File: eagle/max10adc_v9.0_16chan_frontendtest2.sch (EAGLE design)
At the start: 189 parts, among them IC1 MAX11115AUT+T, IC2 MAX11115AUT+T, IC3 OPA4322AIPWR, IC4 MAX11115AUT+T, IC5 MAX11115AUT+T, K1 AQY21SOP, K3 AQY21SOP, K5 AQY21SOP, K6 AQY21SOP, U340G CH340G, X1 LTI-SASF54GT, X4 LTI-SASF54GT, X5 LTI-SASF54GT, X6 LTI-SASF54GT, Y1 ABL-12.000MHZ-B2

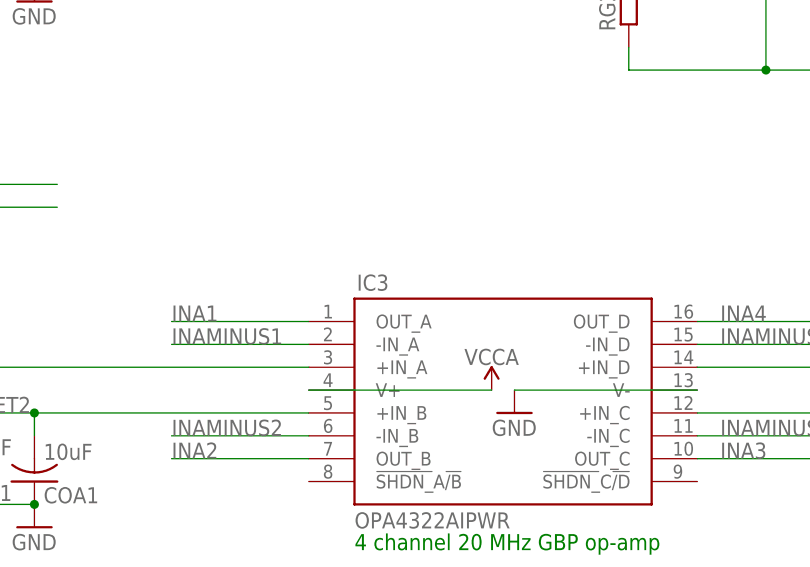
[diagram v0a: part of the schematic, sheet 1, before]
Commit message: 2msps working
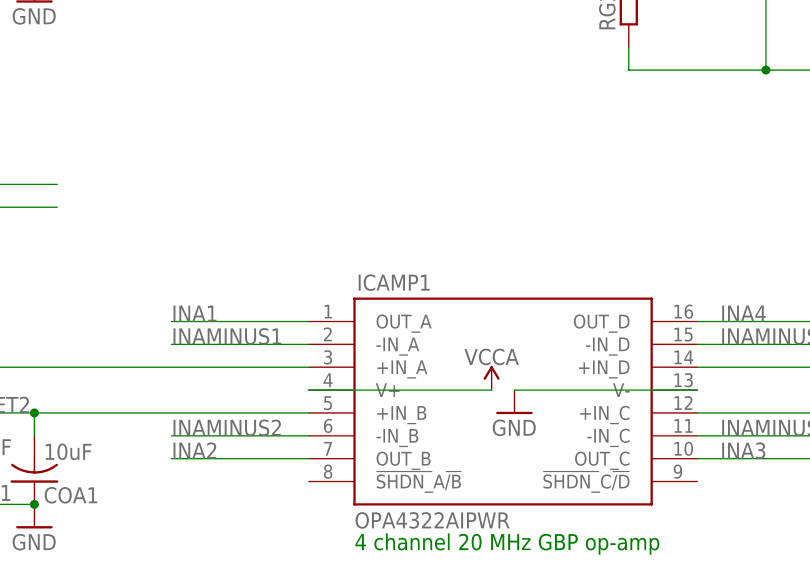
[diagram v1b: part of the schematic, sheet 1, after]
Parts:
- removed IC5: MAX11115AUT+T, SamacSys_Parts:MAX11115AUT+T
- added ICAMP1: OPA4322AIPWR, SamacSys_Parts:OPA4322AIPWR
- IC3: value OPA4322AIPWR -> MAX11115AUT+T; device SamacSys_Parts:OPA4322AIPWR -> SamacSys_Parts:MAX11115AUT+T
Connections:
- net CLKOUT_32: now also IC3.SCLK; no longer IC5.SCLK
- net CLKOUT_33: now also IC3.~CS; no longer IC5.~CS
- net D2A: now also IC3.DOUT; no longer IC5.DOUT
- net GND: now also IC3.GND, ICAMP1.V-; no longer IC3.V-, IC5.GND
- net INA1: now also ICAMP1.OUT_A; no longer IC3.OUT_A
- net INA2: now also ICAMP1.OUT_B; no longer IC3.OUT_B
- net INA3: now also IC3.AIN, ICAMP1.OUT_C; no longer IC3.OUT_C, IC5.AIN
- net INA4: now also ICAMP1.OUT_D; no longer IC3.OUT_D
- net INAMINUS1: now also ICAMP1.-IN_A; no longer IC3.-IN_A
- net INAMINUS2: now also ICAMP1.-IN_B; no longer IC3.-IN_B
- net INAMINUS3: now also ICAMP1.-IN_C; no longer IC3.-IN_C
- net INAMINUS4: now also ICAMP1.-IN_D; no longer IC3.-IN_D
- net OFFSET1: now also ICAMP1.+IN_A; no longer IC3.+IN_A
- net OFFSET2: now also ICAMP1.+IN_B; no longer IC3.+IN_B
- net OFFSET3: now also ICAMP1.+IN_C; no longer IC3.+IN_C
- net OFFSET4: now also ICAMP1.+IN_D; no longer IC3.+IN_D
- net VCCA: now also IC3.VDD, ICAMP1.V+; no longer IC3.V+, IC5.VDD
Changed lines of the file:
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@@
 <part name="GND85" library="supply1" deviceset="GND" device=""/>
 <part name="+3V7" library="supply1" deviceset="+3V3" device=""/>
-<part name="IC3" library="SamacSys_Parts" deviceset="OPA4322AIPWR" device=""/>
+<part name="ICAMP1" library="SamacSys_Parts" deviceset="OPA4322AIPWR" device=""/>
 <part name="IC4" library="SamacSys_Parts" deviceset="MAX11115AUT+T" device=""/>
 <part name="X1" library="con-coax" library_urn="urn:adsk.eagle:library:133" deviceset="LTI-SASF54GT" device="" package3d_urn="urn:adsk.eagle:package:6232/1"/>
@@
 </part>
 <part name="U$5" library="SparkFun-PowerSymbols" library_urn="urn:adsk.eagle:library:530" deviceset="VCCA" device=""/>
-<part name="IC5" library="SamacSys_Parts" deviceset="MAX11115AUT+T" device=""/>
+<part name="IC3" library="SamacSys_Parts" deviceset="MAX11115AUT+T" device=""/>
 <part name="IOEXPAND_0X22" library="microchip" deviceset="MCP23017" device="SS"/>
 <part name="+3V10" library="supply1" deviceset="+3V3" device=""/>
@@
 <attribute name="VALUE" x="86.36" y="233.68" size="1.778" layer="96"/>
 </instance>
-<instance part="IC3" gate="G$1" x="132.08" y="60.96" smashed="yes">
+<instance part="ICAMP1" gate="G$1" x="132.08" y="60.96" smashed="yes">
 <attribute name="NAME" x="137.414" y="65.278" size="1.778" layer="95" align="center-left"/>
 <attribute name="VALUE" x="137.16" y="38.862" size="1.778" layer="96" align="center-left"/>
@@
 </segment>
 <segment>
-<pinref part="IC3" gate="G$1" pin="V-"/>
+<pinref part="ICAMP1" gate="G$1" pin="V-"/>
 <pinref part="GND40" gate="1" pin="GND"/>
 <wire x1="175.26" y1="53.34" x2="154.94" y2="53.34" width="0.1524" layer="91"/>
@@
 </segment>
 <segment>
-<pinref part="IC3" gate="G$1" pin="OUT_A"/>
+<pinref part="ICAMP1" gate="G$1" pin="OUT_A"/>
 <wire x1="132.08" y1="60.96" x2="116.84" y2="60.96" width="0.1524" layer="91"/>
 <label x="116.84" y="60.96" size="1.778" layer="95"/>
@@
 <junction x="68.58" y="55.88"/>
 <label x="78.74" y="55.88" size="1.778" layer="95"/>
-<pinref part="IC3" gate="G$1" pin="+IN_A"/>
+<pinref part="ICAMP1" gate="G$1" pin="+IN_A"/>
 </segment>
 </net>
@@
 </segment>
 <segment>
-<pinref part="IC3" gate="G$1" pin="-IN_A"/>
+<pinref part="ICAMP1" gate="G$1" pin="-IN_A"/>
 <wire x1="132.08" y1="58.42" x2="116.84" y2="58.42" width="0.1524" layer="91"/>
 <label x="116.84" y="58.42" size="1.778" layer="95"/>
@@
 <segment>
 <pinref part="U$7" gate="G$1" pin="VCCA"/>
-<pinref part="IC3" gate="G$1" pin="V+"/>
+<pinref part="ICAMP1" gate="G$1" pin="V+"/>
 <wire x1="152.4" y1="53.34" x2="132.08" y2="53.34" width="0.1524" layer="91"/>
 </segment>
@@
 </segment>
 <segment>
-<pinref part="IC3" gate="G$1" pin="OUT_B"/>
+<pinref part="ICAMP1" gate="G$1" pin="OUT_B"/>
 <wire x1="132.08" y1="45.72" x2="116.84" y2="45.72" width="0.1524" layer="91"/>
 <label x="116.84" y="45.72" size="1.778" layer="95"/>
@@
 </segment>
 <segment>
-<pinref part="IC3" gate="G$1" pin="-IN_B"/>
+<pinref part="ICAMP1" gate="G$1" pin="-IN_B"/>
 <wire x1="132.08" y1="48.26" x2="116.84" y2="48.26" width="0.1524" layer="91"/>
 <label x="116.84" y="48.26" size="1.778" layer="95"/>
@@
 </segment>
 <segment>
-<pinref part="IC3" gate="G$1" pin="OUT_C"/>
+<pinref part="ICAMP1" gate="G$1" pin="OUT_C"/>
 <wire x1="175.26" y1="45.72" x2="190.5" y2="45.72" width="0.1524" layer="91"/>
 <label x="177.8" y="45.72" size="1.778" layer="95"/>
@@
 </segment>
 <segment>
-<pinref part="IC3" gate="G$1" pin="-IN_C"/>
+<pinref part="ICAMP1" gate="G$1" pin="-IN_C"/>
 <wire x1="175.26" y1="48.26" x2="190.5" y2="48.26" width="0.1524" layer="91"/>
 <label x="177.8" y="48.26" size="1.778" layer="95"/>
@@
 </segment>
 <segment>
-<pinref part="IC3" gate="G$1" pin="OUT_D"/>
+<pinref part="ICAMP1" gate="G$1" pin="OUT_D"/>
 <wire x1="175.26" y1="60.96" x2="190.5" y2="60.96" width="0.1524" layer="91"/>
 <label x="177.8" y="60.96" size="1.778" layer="95"/>
@@
 </segment>
 <segment>
-<pinref part="IC3" gate="G$1" pin="-IN_D"/>
+<pinref part="ICAMP1" gate="G$1" pin="-IN_D"/>
 <wire x1="175.26" y1="58.42" x2="190.5" y2="58.42" width="0.1524" layer="91"/>
 <label x="177.8" y="58.42" size="1.778" layer="95"/>
@@
 <junction x="220.98" y="55.88"/>
 <label x="220.98" y="55.88" size="1.778" layer="95"/>
-<pinref part="IC3" gate="G$1" pin="+IN_D"/>
+<pinref part="ICAMP1" gate="G$1" pin="+IN_D"/>
 <wire x1="220.98" y1="55.88" x2="175.26" y2="55.88" width="0.1524" layer="91"/>
 </segment>
@@
 <junction x="198.12" y="50.8"/>
 <label x="198.12" y="50.8" size="1.778" layer="95"/>
-<pinref part="IC3" gate="G$1" pin="+IN_C"/>
+<pinref part="ICAMP1" gate="G$1" pin="+IN_C"/>
 <wire x1="175.26" y1="50.8" x2="198.12" y2="50.8" width="0.1524" layer="91"/>
 </segment>
@@
 <junction x="91.44" y="50.8"/>
 <label x="91.44" y="50.8" size="1.778" layer="95"/>
-<pinref part="IC3" gate="G$1" pin="+IN_B"/>
+<pinref part="ICAMP1" gate="G$1" pin="+IN_B"/>
 <wire x1="132.08" y1="50.8" x2="101.6" y2="50.8" width="0.1524" layer="91"/>
 <junction x="101.6" y="50.8"/>
@@
 <attribute name="VALUE" x="33.02" y="193.294" size="1.778" layer="96" align="bottom-center"/>
 </instance>
-<instance part="IC5" gate="G$1" x="38.1" y="190.5" smashed="yes">
+<instance part="IC3" gate="G$1" x="38.1" y="190.5" smashed="yes">
 <attribute name="NAME" x="44.45" y="198.12" size="1.778" layer="95" align="center-left"/>
 <attribute name="VALUE" x="44.45" y="195.58" size="1.778" layer="96" align="center-left"/>
@@
 <pinref part="GND17" gate="1" pin="GND"/>
 <wire x1="38.1" y1="187.96" x2="27.94" y2="187.96" width="0.1524" layer="91"/>
-<pinref part="IC5" gate="G$1" pin="GND"/>
+<pinref part="IC3" gate="G$1" pin="GND"/>
 <wire x1="27.94" y1="187.96" x2="25.4" y2="187.96" width="0.1524" layer="91"/>
 <wire x1="12.7" y1="187.96" x2="25.4" y2="187.96" width="0.1524" layer="91"/>
@@
 <wire x1="66.04" y1="190.5" x2="81.28" y2="190.5" width="0.1524" layer="91"/>
 <label x="68.58" y="190.5" size="1.778" layer="95"/>
-<pinref part="IC5" gate="G$1" pin="SCLK"/>
+<pinref part="IC3" gate="G$1" pin="SCLK"/>
 <wire x1="66.04" y1="190.5" x2="81.28" y2="190.5" width="0.1524" layer="91"/>
 <junction x="66.04" y="190.5"/>
@@
 <pinref part="U$5" gate="G$1" pin="VCCA"/>
 <wire x1="38.1" y1="190.5" x2="33.02" y2="190.5" width="0.1524" layer="91"/>
-<pinref part="IC5" gate="G$1" pin="VDD"/>
+<pinref part="IC3" gate="G$1" pin="VDD"/>
 <pinref part="CADD4" gate="G$1" pin="1"/>
 <wire x1="12.7" y1="195.58" x2="27.94" y2="195.58" width="0.1524" layer="91"/>
@@
 </segment>
 <segment>
-<pinref part="IC5" gate="G$1" pin="~CS"/>
+<pinref part="IC3" gate="G$1" pin="~CS"/>
 <wire x1="66.04" y1="185.42" x2="81.28" y2="185.42" width="0.1524" layer="91"/>
 <label x="68.58" y="185.42" size="1.778" layer="95"/>
@@
 <wire x1="33.02" y1="185.42" x2="38.1" y2="185.42" width="0.1524" layer="91"/>
 <label x="33.02" y="182.88" size="1.778" layer="95"/>
-<pinref part="IC5" gate="G$1" pin="AIN"/>
+<pinref part="IC3" gate="G$1" pin="AIN"/>
 </segment>
 </net>
@@
 <wire x1="66.04" y1="187.96" x2="73.66" y2="187.96" width="0.1524" layer="91"/>
 <label x="68.58" y="187.96" size="1.778" layer="95"/>
-<pinref part="IC5" gate="G$1" pin="DOUT"/>
+<pinref part="IC3" gate="G$1" pin="DOUT"/>
 <junction x="66.04" y="187.96"/>
 </segment>

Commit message: 4x less gain and associated compensation, and input 6 pin connector
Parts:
- removed RG1_5, RG1_6, RG3_1, RG3_3: 100k, resistor:R-EU_R0805
- removed RG2_5, RG2_6, RG4_1, RG4_3: 1M, resistor:R-EU_R0805
- added BJ1: 6p-2.54, Seeed-Connector:DIP-BLACK-MALE-HEADER(6P-2.54)
- CGAIN1_1, CGAIN1_3, CGAIN1_5, CGAIN1_6: value 33pF -> 220pF
- CH1, CH3, CH5, CH6: value 3-10pF -> 8-45pF; MPN TZY2Z100AC01 -> TZY2K450AC01
- RG1_1, RG1_3, RG3_5, RG3_6: value 100k -> 47k
- RG2_1, RG2_3, RG4_5, RG4_6: value 1M -> 470k
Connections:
- removed net INJ5: CAC5.2, IN3.2, K5.DS2, S10.2, X4.1
- removed net INJ6: CAC6.2, IN4.2, K6.DS2, S12.2, X6.1
- removed net N$2: RG1_1.1, RG3_1.2
- removed net N$20: RG1_5.1, RG3_5.2
- removed net N$21: RG2_5.1, RG4_5.2
- removed net N$25: RG1_6.1, RG3_6.2
- removed net N$26: RG2_6.1, RG4_6.2
- removed net N$3: RG2_1.1, RG4_1.2
- removed net N$7: RG1_3.1, RG3_3.2
- removed net N$8: RG2_3.1, RG4_3.2
- new net INJ2: BJ1.4, CAC3.2, IN2.2, K3.DS2, S5.2, X5.1
- new net INJ4: BJ1.2, CAC6.2, IN4.2, K6.DS2, S12.2, X6.1
- net CGAIN1: now also RG1_1.1; no longer RG3_1.1
- net CGAIN2: now also RG2_1.1; no longer RG4_1.1
- net CGAIN5: now also RG1_3.1; no longer RG3_3.1
- net CGAIN6: now also RG2_3.1; no longer RG4_3.1
- net GND: now also BJ1.1
- net INAMINUS3: now also RG3_5.2, RG4_5.2; no longer RG1_5.2, RG2_5.2
- net INAMINUS4: now also RG3_6.2, RG4_6.2; no longer RG1_6.2, RG2_6.2
- net INJ1: now also BJ1.5
- net INJ3: now also BJ1.3, CAC5.2, IN3.2, K5.DS2, S10.2, X4.1; no longer CAC3.2, IN2.2, K3.DS2, S5.2, X5.1
- net VCCA: now also BJ1.6

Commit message: routed for MF
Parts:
- added ACR10, ACR11, ACR12, ACR13, ACR14, ACR15, ACR16, ACR21, ACR22, ACR23, ACR24, ACR9: 560, resistor:R-EU_R0805
- added BJ2, BJ3, BJ4: 6p-2.54, Seeed-Connector:DIP-BLACK-MALE-HEADER(6P-2.54)
- added C5VOPAMP3, C5VOPAMP4, C5VOPAMP6, CADD10, CADD11, CADD12, CADD13, CADD14, CADD15, CADD16, CADD21, CADD22, CADD23, CADD24, CADD9, COB10, COB11, COB12, COB13, COB14, COB15, COB16, COB21, COB22, COB23, COB24, COB9, COFFSET2, COFFSET3, COFFSET5: 0.1uF, rcl:C-EUC0805K
- added CAC10, CAC11, CAC12, CAC13, CAC14, CAC15, CAC16, CAC21, CAC22, CAC23, CAC24, CAC9: 0.01uF, rcl@1:C-USC0603
- added CGAIN1_10, CGAIN1_11, CGAIN1_12, CGAIN1_13, CGAIN1_14, CGAIN1_15, CGAIN1_16, CGAIN1_21, CGAIN1_22, CGAIN1_23, CGAIN1_24, CGAIN1_9: 220pF, rcl@1:C-USC0603
- added CH10, CH11, CH12, CH13, CH14, CH15, CH16, CH2, CH4, CH7, CH8, CH9, CL10, CL11, CL12, CL13, CL14, CL15, CL16, CL2, CL4, CL7, CL8, CL9: 8-45pF, SparkFun-Passives:CAP_ADJSMD
- added CIN10, CIN11, CIN12, CIN13, CIN14, CIN15, CIN16, CIN21, CIN22, CIN23, CIN24, CIN9: 10pF, rcl@1:C-USC0603
- added CIN56S10, CIN56S11, CIN56S12, CIN56S13, CIN56S14, CIN56S15, CIN56S16, CIN56S21, CIN56S22, CIN56S23, CIN56S24, CIN56S9: 56pF, rcl@1:C-USC0603
- added CINS10, CINS11, CINS12, CINS13, CINS14, CINS15, CINS16, CINS21, CINS22, CINS23, CINS24, CINS9: 1nF, rcl@1:C-USC0603
- added COA10, COA11, COA12, COA13, COA14, COA15, COA16, COA21, COA22, COA23, COA24, COA9: 10uF, rcl@1:C-USC1206
- added DAC2, DAC3, DAC4: MCP4728, Luca Eagle-Library:MCP4728
- added GSW10, GSW11, GSW12, GSW13, GSW14, GSW15, GSW16, GSW21, GSW22, GSW23, GSW24, GSW9: 741G3157DBVR, 74xx-little-us:741G3157DBVR
- added IC10, IC11, IC12, IC13, IC14, IC15, IC16, IC21, IC22, IC23, IC24, IC9: MAX11115AUT+T, SamacSys_Parts:MAX11115AUT+T
- added ICAMP3, ICAMP4, ICAMP6: OPA4322AIPWR, SamacSys_Parts:OPA4322AIPWR
- added IN10, IN11, IN12, IN13, IN14, IN15, IN16, IN5, IN6, IN7, IN8, IN9: 2p-2.54, Seeed-Connector:DIP-BLACK-MALE-HEADER-VERT(2P-2.54)
- added K10, K11, K12, K13, K14, K15, K16, K21, K22, K23, K24, K9: AQY21SOP, relay:AQY21SOP
- added R50-33, R50-34, R50-35, R50-36, R50-37, R50-38, R50-39, R50-40, R50-41, R50-42, R50-43, R50-44, R50-45, R50-46, R50-47, R50-48, R50-49, R50-50, R50-51, R50-52, R50-53, R50-54, R50-55, R50-56, R50-57, R50-58, R50-59, R50-60, R50-61, R50-62, R50-63, R50-64, R50-81, R50-82, R50-83, R50-84, R50-85, R50-86, R50-87, R50-88, R50-89, R50-90, R50-91, R50-92, R50-93, R50-94, R50-95, R50-96: 200R, resistor:R-EU_R0805
- added RG1_11, RG1_12, RG1_5, RG1_6, RG1_7, RG1_8, RG3_11, RG3_12, RG3_3, RG3_4, RG3_7, RG3_8: 47k, resistor:R-EU_R0805
- added RG2_11, RG2_12, RG2_5, RG2_6, RG2_7, RG2_8, RG4_11, RG4_12, RG4_3, RG4_4, RG4_7, RG4_8: 470k, resistor:R-EU_R0805
- added RIN10, RIN11, RIN12, RIN13, RIN14, RIN15, RIN16, RIN21, RIN22, RIN23, RIN24, RIN9: 1.1M, resistor:R-EU_R0805
- added RIN10M10, RIN10M11, RIN10M12, RIN10M13, RIN10M14, RIN10M15, RIN10M16, RIN10M21, RIN10M22, RIN10M23, RIN10M24, RIN10M9: 10M, resistor:R-EU_R0805
- added RINS10, RINS11, RINS12, RINS13, RINS14, RINS15, RINS16, RINS21, RINS22, RINS23, RINS24, RINS9: 11K, resistor:R-EU_R0805
- added ROFFSET10, ROFFSET11, ROFFSET12, ROFFSET13, ROFFSET14, ROFFSET15, ROFFSET16, ROFFSET21, ROFFSET22, ROFFSET23, ROFFSET24, ROFFSET9: 200, resistor:R-EU_R0805
- added S18, S19, S20, S21, S22, S23, S24, S25, S26, S27, S28, S29, S30, S31, S32, S33, S42, S43, S44, S45, S46, S47, S48, S49: JS202011SCQN, switch-ck:JS202011SCQN
- added X10, X11, X12, X13, X14, X15, X16, X21, X22, X23, X24, X9: LTI-SASF54GT, con-coax:LTI-SASF54GT
- renumbered RLEDPOW to RPOW
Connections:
- new net CGAIN17: CGAIN1_9.2, CL5.4, GSW9G$1.A, RG1_5.1
- new net CGAIN18: CH5.4, GSW9G$1.B, RG2_5.1
- new net CGAIN19: CGAIN1_10.2, CL6.4, GSW10G$1.A, RG1_6.1
- new net CGAIN20: CH6.4, GSW10G$1.B, RG2_6.1
- new net CGAIN21: CGAIN1_11.2, CL7.4, GSW11G$1.A, RG3_3.1
- new net CGAIN22: CH7.4, GSW11G$1.B, RG4_3.1
- new net CGAIN23: CGAIN1_12.2, CL8.4, GSW12G$1.A, RG3_4.1
- new net CGAIN24: CH8.4, GSW12G$1.B, RG4_4.1
- new net CGAIN25: CGAIN1_13.2, CL9.4, GSW13G$1.A, RG1_7.1
- new net CGAIN26: CH9.4, GSW13G$1.B, RG2_7.1
- new net CGAIN27: CGAIN1_14.2, CL10.4, GSW14G$1.A, RG1_8.1
- new net CGAIN28: CH10.4, GSW14G$1.B, RG2_8.1
- new net CGAIN29: CGAIN1_15.2, CL11.4, GSW15G$1.A, RG3_7.1
- new net CGAIN30: CH11.4, GSW15G$1.B, RG4_7.1
- new net CGAIN31: CGAIN1_16.2, CL12.4, GSW16G$1.A, RG3_8.1
- new net CGAIN32: CH12.4, GSW16G$1.B, RG4_8.1
- new net CGAIN41: CGAIN1_21.2, CL13.4, GSW21G$1.A, RG1_11.1
- new net CGAIN42: CH13.4, GSW21G$1.B, RG2_11.1
- new net CGAIN43: CGAIN1_22.2, CL14.4, GSW22G$1.A, RG1_12.1
- new net CGAIN44: CH14.4, GSW22G$1.B, RG2_12.1
- new net CGAIN45: CGAIN1_23.2, CL15.4, GSW23G$1.A, RG3_11.1
- new net CGAIN46: CH15.4, GSW23G$1.B, RG4_11.1
- new net CGAIN47: CGAIN1_24.2, CL16.4, GSW24G$1.A, RG3_12.1
- new net CGAIN48: CH16.4, GSW24G$1.B, RG4_12.1
- new net INA10: GSW14G$1.X, IC15.AIN, ICAMP4.OUT_B
- new net INA11: GSW15G$1.X, IC16.AIN, ICAMP4.OUT_C
- new net INA12: GSW16G$1.X, IC13.AIN, ICAMP4.OUT_D
- new net INA13: GSW21G$1.X, IC22.AIN, ICAMP6.OUT_A
- new net INA14: GSW22G$1.X, IC23.AIN, ICAMP6.OUT_B
- new net INA15: GSW23G$1.X, IC24.AIN, ICAMP6.OUT_C
- new net INA16: GSW24G$1.X, IC21.AIN, ICAMP6.OUT_D
- new net INA5: GSW9G$1.X, IC10.AIN, ICAMP3.OUT_A
- new net INA6: GSW10G$1.X, IC11.AIN, ICAMP3.OUT_B
- new net INA7: GSW11G$1.X, IC12.AIN, ICAMP3.OUT_C
- new net INA8: GSW12G$1.X, IC9.AIN, ICAMP3.OUT_D
- new net INA9: GSW13G$1.X, IC14.AIN, ICAMP4.OUT_A
- new net INAMINUS10: CGAIN1_14.1, CH10.3, CIN14.2, CIN56S14.2, CINS14.2, CL10.3, ICAMP4.-IN_B, RG1_8.2, RG2_8.2, RIN14.2, RINS14.2
- new net INAMINUS11: CGAIN1_15.1, CH11.3, CIN15.2, CIN56S15.2, CINS15.2, CL11.3, ICAMP4.-IN_C, RG3_7.2, RG4_7.2, RIN15.2, RINS15.2
- new net INAMINUS12: CGAIN1_16.1, CH12.3, CIN16.2, CIN56S16.2, CINS16.2, CL12.3, ICAMP4.-IN_D, RG3_8.2, RG4_8.2, RIN16.2, RINS16.2
- new net INAMINUS13: CGAIN1_21.1, CH13.3, CIN21.2, CIN56S21.2, CINS21.2, CL13.3, ICAMP6.-IN_A, RG1_11.2, RG2_11.2, RIN21.2, RINS21.2
- new net INAMINUS14: CGAIN1_22.1, CH14.3, CIN22.2, CIN56S22.2, CINS22.2, CL14.3, ICAMP6.-IN_B, RG1_12.2, RG2_12.2, RIN22.2, RINS22.2
- new net INAMINUS15: CGAIN1_23.1, CH15.3, CIN23.2, CIN56S23.2, CINS23.2, CL15.3, ICAMP6.-IN_C, RG3_11.2, RG4_11.2, RIN23.2, RINS23.2
- new net INAMINUS16: CGAIN1_24.1, CH16.3, CIN24.2, CIN56S24.2, CINS24.2, CL16.3, ICAMP6.-IN_D, RG3_12.2, RG4_12.2, RIN24.2, RINS24.2
- new net INAMINUS5: CGAIN1_9.1, CH5.3, CIN56S9.2, CIN9.2, CINS9.2, CL5.3, ICAMP3.-IN_A, RG1_5.2, RG2_5.2, RIN9.2, RINS9.2
- new net INAMINUS6: CGAIN1_10.1, CH6.3, CIN10.2, CIN56S10.2, CINS10.2, CL6.3, ICAMP3.-IN_B, RG1_6.2, RG2_6.2, RIN10.2, RINS10.2
- new net INAMINUS7: CGAIN1_11.1, CH7.3, CIN11.2, CIN56S11.2, CINS11.2, CL7.3, ICAMP3.-IN_C, RG3_3.2, RG4_3.2, RIN11.2, RINS11.2
- new net INAMINUS8: CGAIN1_12.1, CH8.3, CIN12.2, CIN56S12.2, CINS12.2, CL8.3, ICAMP3.-IN_D, RG3_4.2, RG4_4.2, RIN12.2, RINS12.2
- new net INAMINUS9: CGAIN1_13.1, CH9.3, CIN13.2, CIN56S13.2, CINS13.2, CL9.3, ICAMP4.-IN_A, RG1_7.2, RG2_7.2, RIN13.2, RINS13.2
- new net INJ10: BJ3.4, CAC14.2, IN10.2, K14.DS2, S28.2, X14.1
- new net INJ11: BJ3.3, CAC15.2, IN11.2, K15.DS2, S30.2, X15.1
- new net INJ12: BJ3.2, CAC16.2, IN12.2, K16.DS2, S32.2, X16.1
- new net INJ13: BJ4.5, CAC21.2, IN13.2, K21.DS2, S42.2, X21.1
- new net INJ14: BJ4.4, CAC22.2, IN14.2, K22.DS2, S44.2, X22.1
- new net INJ15: BJ4.3, CAC23.2, IN15.2, K23.DS2, S46.2, X23.1
- new net INJ16: BJ4.2, CAC24.2, IN16.2, K24.DS2, S48.2, X24.1
- new net INJ5: BJ2.5, CAC9.2, IN5.2, K9.DS2, S18.2, X9.1
- new net INJ6: BJ2.4, CAC10.2, IN6.2, K10.DS2, S20.2, X10.1
- new net INJ7: BJ2.3, CAC11.2, IN7.2, K11.DS2, S22.2, X11.1
- new net INJ8: BJ2.2, CAC12.2, IN8.2, K12.DS2, S24.2, X12.1
- new net INJ9: BJ3.5, CAC13.2, IN9.2, K13.DS2, S26.2, X13.1
- new net N$15: DAC2.VOUT_A, ROFFSET9.2
- new net N$16: DAC2.VOUT_B, ROFFSET10.2
- new net N$17: DAC2.VOUT_C, ROFFSET11.2
- new net N$19: DAC2.VOUT_D, ROFFSET12.2
- new net N$2: ACR11.2, K10.A
- new net N$20: DAC3.VOUT_A, ROFFSET13.2
- new net N$21: DAC3.VOUT_B, ROFFSET14.2
- new net N$22: DAC3.VOUT_C, ROFFSET15.2
- new net N$25: DAC3.VOUT_D, ROFFSET16.2
- new net N$28: CAC9.1, K9.DS1, RIN10M9.1, S19.2
- new net N$29: CAC10.1, K10.DS1, RIN10M10.1, S21.2
- new net N$3: ACR10.2, K11.A
- new net N$30: CAC11.1, K11.DS1, RIN10M11.1, S23.2
- new net N$32: CAC12.1, K12.DS1, RIN10M12.1, S25.2
- new net N$37: ACR15.2, K14.A
- new net N$38: ACR14.2, K15.A
- new net N$39: ACR16.2, K16.A
- new net N$40: ACR21.2, K21.A
- new net N$41: DAC4.VOUT_A, ROFFSET21.2
- new net N$42: DAC4.VOUT_B, ROFFSET22.2
- new net N$43: DAC4.VOUT_C, ROFFSET23.2
- new net N$50: DAC4.VOUT_D, ROFFSET24.2
- new net N$52: CAC13.1, K13.DS1, RIN10M13.1, S27.2
- new net N$53: CAC14.1, K14.DS1, RIN10M14.1, S29.2
- new net N$54: CAC15.1, K15.DS1, RIN10M15.1, S31.2
- new net N$55: CAC16.1, K16.DS1, RIN10M16.1, S33.2
- new net N$59: ACR23.2, K22.A
- new net N$60: ACR22.2, K23.A
- new net N$61: ACR24.2, K24.A
- new net N$62: ACR9.2, K9.A
- new net N$68: CAC21.1, K21.DS1, RIN10M21.1, S43.2
- new net N$69: CAC22.1, K22.DS1, RIN10M22.1, S45.2
- new net N$7: ACR12.2, K12.A
- new net N$70: CAC23.1, K23.DS1, RIN10M23.1, S47.2
- new net N$71: CAC24.1, K24.DS1, RIN10M24.1, S49.2
- new net N$8: ACR13.2, K13.A
- new net N50_10: R50-53.1, R50-54.1, R50-55.1, R50-56.1, S28.3
- new net N50_11: R50-57.1, R50-58.1, R50-59.1, R50-60.1, S30.3
- new net N50_12: R50-61.1, R50-62.1, R50-63.1, R50-64.1, S32.3
- new net N50_13: R50-81.1, R50-82.1, R50-83.1, R50-84.1, S42.3
- new net N50_14: R50-85.1, R50-86.1, R50-87.1, R50-88.1, S44.3
- new net N50_15: R50-89.1, R50-90.1, R50-91.1, R50-92.1, S46.3
- new net N50_16: R50-93.1, R50-94.1, R50-95.1, R50-96.1, S48.3
- new net N50_5: R50-33.1, R50-34.1, R50-35.1, R50-36.1, S18.3
- new net N50_6: R50-37.1, R50-38.1, R50-39.1, R50-40.1, S20.3
- new net N50_7: R50-41.1, R50-42.1, R50-43.1, R50-44.1, S22.3
- new net N50_8: R50-45.1, R50-46.1, R50-47.1, R50-48.1, S24.3
- new net N50_9: R50-49.1, R50-50.1, R50-51.1, R50-52.1, S26.3
- new net NNG_10: CIN14.1, RIN14.1, S29.3
- new net NNG_11: CIN15.1, RIN15.1, S31.3
- new net NNG_12: CIN16.1, RIN16.1, S33.3
- new net NNG_13: CIN21.1, RIN21.1, S43.3
- new net NNG_14: CIN22.1, RIN22.1, S45.3
- new net NNG_15: CIN23.1, RIN23.1, S47.3
- new net NNG_16: CIN24.1, RIN24.1, S49.3
- new net NNG_5: CIN9.1, RIN9.1, S19.3
- new net NNG_6: CIN10.1, RIN10.1, S21.3
- new net NNG_7: CIN11.1, RIN11.1, S23.3
- new net NNG_8: CIN12.1, RIN12.1, S25.3
- new net NNG_9: CIN13.1, RIN13.1, S27.3
- new net NSG_10: CIN56S14.1, CINS14.1, RINS14.1, S29.1
- new net NSG_11: CIN56S15.1, CINS15.1, RINS15.1, S31.1
- new net NSG_12: CIN56S16.1, CINS16.1, RINS16.1, S33.1
- new net NSG_13: CIN56S21.1, CINS21.1, RINS21.1, S43.1
- new net NSG_14: CIN56S22.1, CINS22.1, RINS22.1, S45.1
- new net NSG_15: CIN56S23.1, CINS23.1, RINS23.1, S47.1
- new net NSG_16: CIN56S24.1, CINS24.1, RINS24.1, S49.1
- new net NSG_5: CIN56S9.1, CINS9.1, RINS9.1, S19.1
- new net NSG_6: CIN56S10.1, CINS10.1, RINS10.1, S21.1
- new net NSG_7: CIN56S11.1, CINS11.1, RINS11.1, S23.1
- new net NSG_8: CIN56S12.1, CINS12.1, RINS12.1, S25.1
- new net NSG_9: CIN56S13.1, CINS13.1, RINS13.1, S27.1
- new net OFFSET10: COA14.2, COB14.2, ICAMP4.+IN_B, ROFFSET14.1
- new net OFFSET11: COA15.2, COB15.2, ICAMP4.+IN_C, ROFFSET15.1
- new net OFFSET12: COA16.2, COB16.2, ICAMP4.+IN_D, ROFFSET16.1
- new net OFFSET13: COA21.2, COB21.2, ICAMP6.+IN_A, ROFFSET21.1
- new net OFFSET14: COA22.2, COB22.2, ICAMP6.+IN_B, ROFFSET22.1
- new net OFFSET15: COA23.2, COB23.2, ICAMP6.+IN_C, ROFFSET23.1
- new net OFFSET16: COA24.2, COB24.2, ICAMP6.+IN_D, ROFFSET24.1
- new net OFFSET5: COA9.2, COB9.2, ICAMP3.+IN_A, ROFFSET9.1
- new net OFFSET6: COA10.2, COB10.2, ICAMP3.+IN_B, ROFFSET10.1
- new net OFFSET7: COA11.2, COB11.2, ICAMP3.+IN_C, ROFFSET11.1
- new net OFFSET8: COA12.2, COB12.2, ICAMP3.+IN_D, ROFFSET12.1
- new net OFFSET9: COA13.2, COB13.2, ICAMP4.+IN_A, ROFFSET13.1
- net CGAIN10: now also CH3.4; no longer CH5.4
- net CGAIN11: now also CL4.4; no longer CL6.4
- net CGAIN12: now also CH4.4; no longer CH6.4
- net CGAIN5: now also CL2.4; no longer CL3.4
- net CGAIN6: now also CH2.4; no longer CH3.4
- net CGAIN9: now also CL3.4; no longer CL5.4
- net CLKOUT_32: now also IC10.SCLK, IC11.SCLK, IC12.SCLK, IC13.SCLK, IC14.SCLK, IC15.SCLK, IC16.SCLK, IC21.SCLK, IC22.SCLK, IC23.SCLK, IC24.SCLK, IC9.SCLK
- net CLKOUT_33: now also IC10.~CS, IC11.~CS, IC12.~CS, IC13.~CS, IC14.~CS, IC15.~CS, IC16.~CS, IC21.~CS, IC22.~CS, IC23.~CS, IC24.~CS, IC9.~CS
- net D0B: now also IC14.DOUT
- net D1B: now also IC15.DOUT
- net D2B: now also IC16.DOUT
- net D3B: now also IC13.DOUT
- net D4A: now also IC10.DOUT
- net D4B: now also IC22.DOUT
- net D5A: now also IC11.DOUT
- net D5B: now also IC23.DOUT
- net D6A: now also IC12.DOUT
- net D6B: now also IC24.DOUT
- net D7A: now also IC9.DOUT
- net D7B: now also IC21.DOUT
- net E_50SW10: now also S28.5
- net E_50SW11: now also S30.5
- net E_50SW12: now also S32.5
- net E_50SW13: now also S42.5
- net E_50SW14: now also S44.5
- net E_50SW15: now also S46.5
- net E_50SW16: now also S48.5
- net E_50SW5: now also S18.5
- net E_50SW6: now also S20.5
- net E_50SW7: now also S22.5
- net E_50SW8: now also S24.5
- net E_50SW9: now also S26.5
- net E_ACSW10: now also ACR15.1
- net E_ACSW11: now also ACR14.1
- net E_ACSW12: now also ACR16.1
- net E_ACSW13: now also ACR21.1
- net E_ACSW14: now also ACR23.1
- net E_ACSW15: now also ACR22.1
- net E_ACSW16: now also ACR24.1
- net E_ACSW5: now also ACR9.1
- net E_ACSW6: now also ACR11.1
- net E_ACSW7: now also ACR10.1
- net E_ACSW8: now also ACR12.1
- net E_ACSW9: now also ACR13.1
- net E_GSW10: now also GSW14G$1.!A!/B
- net E_GSW11: now also GSW15G$1.!A!/B
- net E_GSW12: now also GSW16G$1.!A!/B
- net E_GSW13: now also GSW21G$1.!A!/B
- net E_GSW14: now also GSW22G$1.!A!/B
- net E_GSW15: now also GSW23G$1.!A!/B
- net E_GSW16: now also GSW24G$1.!A!/B
- net E_GSW5: now also GSW9G$1.!A!/B
- net E_GSW6: now also GSW10G$1.!A!/B
- net E_GSW7: now also GSW11G$1.!A!/B
- net E_GSW8: now also GSW12G$1.!A!/B
- net E_GSW9: now also GSW13G$1.!A!/B
- net E_SS10: now also S29.5
- net E_SS11: now also S31.5
- net E_SS12: now also S33.5
- net E_SS13: now also S43.5
- net E_SS14: now also S45.5
- net E_SS15: now also S47.5
- net E_SS16: now also S49.5
- net E_SS5: now also S19.5
- net E_SS6: now also S21.5
- net E_SS7: now also S23.5
- net E_SS8: now also S25.5
- net E_SS9: now also S27.5
- net GND: now also BJ2.1, BJ3.1, BJ4.1, C5VOPAMP3.2, C5VOPAMP4.2, C5VOPAMP6.2, CADD10.2, CADD11.2, CADD12.2, CADD13.2, CADD14.2, CADD15.2, CADD16.2, CADD21.2, CADD22.2, CADD23.2, CADD24.2, CADD9.2, COA10.1, COA11.1, COA12.1, COA13.1, COA14.1, COA15.1, COA16.1, COA21.1, COA22.1, COA23.1, COA24.1, COA9.1, COB10.1, COB11.1, COB12.1, COB13.1, COB14.1, COB15.1, COB16.1, COB21.1, COB22.1, COB23.1, COB24.1, COB9.1, COFFSET2.1, COFFSET3.1, COFFSET5.1, DAC2.!LDAC, DAC2.VSS, DAC3.!LDAC, DAC3.VSS, DAC4.!LDAC, DAC4.VSS, GSW10P.GND, GSW11P.GND, GSW12P.GND, GSW13P.GND, GSW14P.GND, GSW15P.GND, GSW16P.GND, GSW21P.GND, GSW22P.GND, GSW23P.GND, GSW24P.GND, GSW9P.GND, IC10.GND, IC11.GND, IC12.GND, IC13.GND, IC14.GND, IC15.GND, IC16.GND, IC21.GND, IC22.GND, IC23.GND, IC24.GND, IC9.GND, ICAMP3.V-, ICAMP4.V-, ICAMP6.V-, IN10.1, IN11.1, IN12.1, IN13.1, IN14.1, IN15.1, IN16.1, IN5.1, IN6.1, IN7.1, IN8.1, IN9.1, K10.K, K11.K, K12.K, K13.K, K14.K, K15.K, K16.K, K21.K, K22.K, K23.K, K24.K, K9.K, R50-33.2, R50-34.2, R50-35.2, R50-36.2, R50-37.2, R50-38.2, R50-39.2, R50-40.2, R50-41.2, R50-42.2, R50-43.2, R50-44.2, R50-45.2, R50-46.2, R50-47.2, R50-48.2, R50-49.2, R50-50.2, R50-51.2, R50-52.2, R50-53.2, R50-54.2, R50-55.2, R50-56.2, R50-57.2, R50-58.2, R50-59.2, R50-60.2, R50-61.2, R50-62.2, R50-63.2, R50-64.2, R50-81.2, R50-82.2, R50-83.2, R50-84.2, R50-85.2, R50-86.2, R50-87.2, R50-88.2, R50-89.2, R50-90.2, R50-91.2, R50-92.2, R50-93.2, R50-94.2, R50-95.2, R50-96.2, RIN10M10.2, RIN10M11.2, RIN10M12.2, RIN10M13.2, RIN10M14.2, RIN10M15.2, RIN10M16.2, RIN10M21.2, RIN10M22.2, RIN10M23.2, RIN10M24.2, RIN10M9.2, S18.6, S19.6, S20.6, S21.6, S22.6, S23.6, S24.6, S25.6, S26.6, S27.6, S28.6, S29.6, S30.6, S31.6, S32.6, S33.6, S42.6, S43.6, S44.6, S45.6, S46.6, S47.6, S48.6, S49.6, X10.2, X11.2, X12.2, X13.2, X14.2, X15.2, X16.2, X21.2, X22.2, X23.2, X24.2, X9.2
- net INAMINUS2: now also CH2.3, CL2.3; no longer CH3.3, CL3.3
- net INAMINUS3: now also CH3.3, CL3.3; no longer CH5.3, CL5.3
- net INAMINUS4: now also CH4.3, CL4.3; no longer CH6.3, CL6.3
- net L141_SCL: now also DAC2.SCL, DAC3.SCL, DAC4.SCL
- net L21_SDA: now also DAC2.SDA, DAC3.SDA, DAC4.SDA
- net VCCA: now also BJ2.6, BJ3.6, BJ4.6, C5VOPAMP3.1, C5VOPAMP4.1, C5VOPAMP6.1, CADD10.1, CADD11.1, CADD12.1, CADD13.1, CADD14.1, CADD15.1, CADD16.1, CADD21.1, CADD22.1, CADD23.1, CADD24.1, CADD9.1, COFFSET2.2, COFFSET3.2, COFFSET5.2, DAC2.VDD, DAC3.VDD, DAC4.VDD, GSW10P.VCC, GSW11P.VCC, GSW12P.VCC, GSW13P.VCC, GSW14P.VCC, GSW15P.VCC, GSW16P.VCC, GSW21P.VCC, GSW22P.VCC, GSW23P.VCC, GSW24P.VCC, GSW9P.VCC, IC10.VDD, IC11.VDD, IC12.VDD, IC13.VDD, IC14.VDD, IC15.VDD, IC16.VDD, IC21.VDD, IC22.VDD, IC23.VDD, IC24.VDD, IC9.VDD, ICAMP3.V+, ICAMP4.V+, ICAMP6.V+
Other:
- note added: "Op Amp"
- moved on the sheet: CH3, CH5, CH6, CL3, CL5, CL6
